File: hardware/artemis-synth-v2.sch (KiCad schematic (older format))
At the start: 41 parts, among them IC1 ATMEGA328P, J1 AVR-ISP-6, J2 CONN JACK STEREO R/A 3PIN 3.5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, SW1 SWITCH_PUSH_CW, SW10 SWITCH_PUSH_CW, SW2 SWITCH_PUSH_CW, SW3 SWITCH_PUSH_CW, SW4 SWITCH_PUSH_CW, SW5 SWITCH_PUSH_CW, SW6 SWITCH_PUSH_CW, SW7 SWITCH_PUSH_CW, SW8 SWITCH_PUSH_CW, SW9 SWITCH_PUSH_CW, U1 MCP4921

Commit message: Updated naming
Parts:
- C1: footprint (none) -> C1V8
- C6: footprint C1 -> C1V8
- D1, D2: footprint (none) -> LED-3MM
- D10, D3, D4, D5, D6, D7, D8, D9: footprint LED-5MM -> LED-3MM
- J2: footprint (none) -> 3-Pin
- R1, R2, R3, R4, R5, R6, R7, R8, R9: footprint (none) -> R4
- RV1: footprint (none) -> THUMBWHEEL_POT_3352T
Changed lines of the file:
@@
-EESchema Schematic File Version 2  date Wed 03 Jul 2013 03:39:44 PM EDT
+EESchema Schematic File Version 2  date Wed 03 Jul 2013 05:09:10 PM EDT
 LIBS:power
 LIBS:device
@@
 LIBS:contrib
 LIBS:valves
-LIBS:mcp49x1
 LIBS:tda2822m
 LIBS:r_us
 LIBS:pot_us
+LIBS:mcp49x1
+LIBS:battery2
+LIBS:artemis-synth-v1-cache
 LIBS:3-pin_audio_jack
-LIBS:artemis-synth-v1-cache
 EELAYER 27 0
 EELAYER END
@@
 F 0 "D4" H 9425 5950 50  0000 C CNN
 F 1 "LED" H 9425 5750 50  0000 C CNN
-F 2 "LED-5MM" H 9425 5850 50  0001 C CNN
+F 2 "LED-3MM" H 9425 5850 50  0001 C CNN
 	1    9425 5850
 	0    1    1    0
@@
 F 0 "D6" H 9875 5950 50  0000 C CNN
 F 1 "LED" H 9875 5750 50  0000 C CNN
-F 2 "LED-5MM" H 9875 5850 50  0001 C CNN
+F 2 "LED-3MM" H 9875 5850 50  0001 C CNN
 	1    9875 5850
 	0    1    1    0
@@
 F 0 "D8" H 10300 5950 50  0000 C CNN
 F 1 "LED" H 10300 5750 50  0000 C CNN
-F 2 "LED-5MM" H 10300 5850 50  0001 C CNN
+F 2 "LED-3MM" H 10300 5850 50  0001 C CNN
 	1    10300 5850
 	0    1    1    0
@@
 F 0 "D10" H 10775 5950 50  0000 C CNN
 F 1 "LED" H 10775 5750 50  0000 C CNN
-F 2 "LED-5MM" H 10775 5850 50  0001 C CNN
+F 2 "LED-3MM" H 10775 5850 50  0001 C CNN
 	1    10775 5850
 	0    1    1    0
@@
 F 0 "D9" H 10775 5450 50  0000 C CNN
 F 1 "LED" H 10775 5250 50  0000 C CNN
-F 2 "LED-5MM" H 10775 5350 50  0001 C CNN
+F 2 "LED-3MM" H 10775 5350 50  0001 C CNN
 	1    10775 5350
 	0    1    1    0
@@
 F 0 "D7" H 10300 5450 50  0000 C CNN
 F 1 "LED" H 10300 5250 50  0000 C CNN
-F 2 "LED-5MM" H 10300 5350 50  0001 C CNN
+F 2 "LED-3MM" H 10300 5350 50  0001 C CNN
 	1    10300 5350
 	0    1    1    0
@@
 F 0 "D5" H 9875 5450 50  0000 C CNN
 F 1 "LED" H 9875 5250 50  0000 C CNN
-F 2 "LED-5MM" H 9875 5350 50  0001 C CNN
+F 2 "LED-3MM" H 9875 5350 50  0001 C CNN
 	1    9875 5350
 	0    1    1    0
@@
 F 0 "D3" H 9425 5450 50  0000 C CNN
 F 1 "LED" H 9425 5250 50  0000 C CNN
-F 2 "LED-5MM" H 9425 5350 50  0001 C CNN
+F 2 "LED-3MM" H 9425 5350 50  0001 C CNN
 	1    9425 5350
 	0    1    1    0
@@
 	-1   0    0    -1
 $EndComp
-Text Label 1688 5375 0    60   ~ 0
+Text Label 3525 5350 0    60   ~ 0
 BT5
-Text Label 1688 5875 0    60   ~ 0
+Text Label 3575 5850 0    60   ~ 0
 BT6
-Text Label 1688 6400 0    60   ~ 0
+Text Label 3575 6375 0    60   ~ 0
 BT7
-Text Label 1688 6950 0    60   ~ 0
+Text Label 3575 6925 0    60   ~ 0
 BT8
-Text Label 1663 7475 0    60   ~ 0
+Text Label 3550 7450 0    60   ~ 0
 BT9
-Text Label 3388 7450 0    60   ~ 0
+Text Label 1825 7475 0    60   ~ 0
 BT4
-Text Label 3413 6925 0    60   ~ 0
+Text Label 1850 6950 0    60   ~ 0
 BT3
-Text Label 3413 6375 0    60   ~ 0
+Text Label 1850 6400 0    60   ~ 0
 BT2
-Text Label 3413 5850 0    60   ~ 0
+Text Label 1850 5875 0    60   ~ 0
 BT1
-Text Label 3363 5350 0    60   ~ 0
+Text Label 1850 5375 0    60   ~ 0
 BT0
 $Comp
@@
 F 0 "D2" H 6100 5975 50  0000 L CNN
 F 1 "TEPT4400" H 6100 5825 50  0000 L CNN
+F 2 "LED-3MM" H 6100 5925 50  0001 C CNN
 	1    5950 5925
 	-1   0    0    -1
@@
 F 0 "R2" H 5405 6100 50  0000 C CNN
 F 1 "1k" H 5400 5950 50  0000 C CNN
+F 2 "R4" H 5400 6050 50  0001 C CNN
 	1    5250 5975
 	-1   0    0    -1
@@
 F 0 "R3" H 5405 6875 50  0000 C CNN
 F 1 "1k" H 5400 6775 50  0000 C CNN
+F 2 "R4" H 5400 6875 50  0001 C CNN
 	1    5250 6750
 	-1   0    0    -1
@@
 F 0 "R5" H 6005 6900 50  0000 C CNN
 F 1 "47k" H 6025 6800 50  0000 C CNN
+F 2 "R4" H 6025 6900 50  0001 C CNN
 	1    5850 6775
 	-1   0    0    -1
@@
 F 0 "R6" H 6755 1725 50  0000 C CNN
 F 1 "100k" H 6800 1600 50  0000 C CNN
+F 2 "R4" H 6800 1700 50  0001 C CNN
 	1    6600 1600
 	1    0    0    -1
@@
 F 0 "R4" H 5905 3375 50  0000 C CNN
 F 1 "10K" H 5900 3225 50  0000 C CNN
+F 2 "R4" H 5900 3325 50  0001 C CNN
 	1    5750 3250
 	1    0    0    -1
@@
 F 0 "R8" V 8550 2600 50  0000 C CNN
 F 1 "1k" V 8450 2600 50  0000 C CNN
+F 2 "R4" V 8550 2600 50  0001 C CNN
 	1    8300 2525
 	0    -1   -1   0
@@
 F 0 "RV1" H 8455 2900 50  0000 C CNN
 F 1 "1k" H 8475 2800 50  0000 C CNN
+F 2 "THUMBWHEEL_POT_3352T" H 8475 2900 50  0001 C CNN
 	1    8650 2850
 	1    0    0    -1
@@
 F 0 "R7" V 7875 2600 50  0000 C CNN
 F 1 "1k" V 7775 2600 50  0000 C CNN
+F 2 "R4" V 7875 2600 50  0001 C CNN
 	1    7625 2525
 	0    -1   -1   0
@@
 F 0 "C6" V 9075 2925 50  0000 L CNN
 F 1 "33uF" V 8975 2825 50  0000 L CNN
-F 2 "C1" H 9075 2850 50  0001 C CNN
+F 2 "C1V8" H 9075 2850 50  0001 C CNN
 	1    9250 2850
 	0    -1   -1   0
@@
 F 0 "R9" H 9700 3275 50  0000 C CNN
 F 1 "47k" H 9725 3175 50  0000 C CNN
+F 2 "R4" H 9725 3275 50  0001 C CNN
 	1    9550 3200
 	1    0    0    -1
@@
 F 0 "C1" H 2450 1675 50  0000 L CNN
 F 1 "10u" H 2450 1575 50  0000 L CNN
+F 2 "C1V8" H 2450 1675 50  0001 C CNN
 	1    2275 1625
 	1    0    0    -1
@@
 F 0 "D1" V 1400 3275 50  0000 C CNN
 F 1 "GREEN" V 1500 3350 50  0000 C CNN
+F 2 "LED-3MM" V 1600 3350 50  0001 C CNN
 	1    1450 3150
 	0    1    1    0
@@
 F 0 "R1" H 1625 3800 50  0000 C CNN
 F 1 "220" H 1650 3700 50  0000 C CNN
+F 2 "R4" H 1650 3800 50  0001 C CNN
 	1    1450 3700
 	1    0    0    -1
@@
 F 0 "J2" H 10950 3200 60  0000 C CNN
 F 1 "CONN JACK STEREO R/A 3PIN 3.5MM" H 11625 3100 60  0000 C CNN
+F 2 "3-Pin" H 11625 3200 60  0001 C CNN
 F 4 "SJ1-3523N" H 10950 2850 60  0001 C CNN "Manufacture Part Number"
 F 5 "CUI Inc." H 10950 2850 60  0001 C CNN "Manufacture"

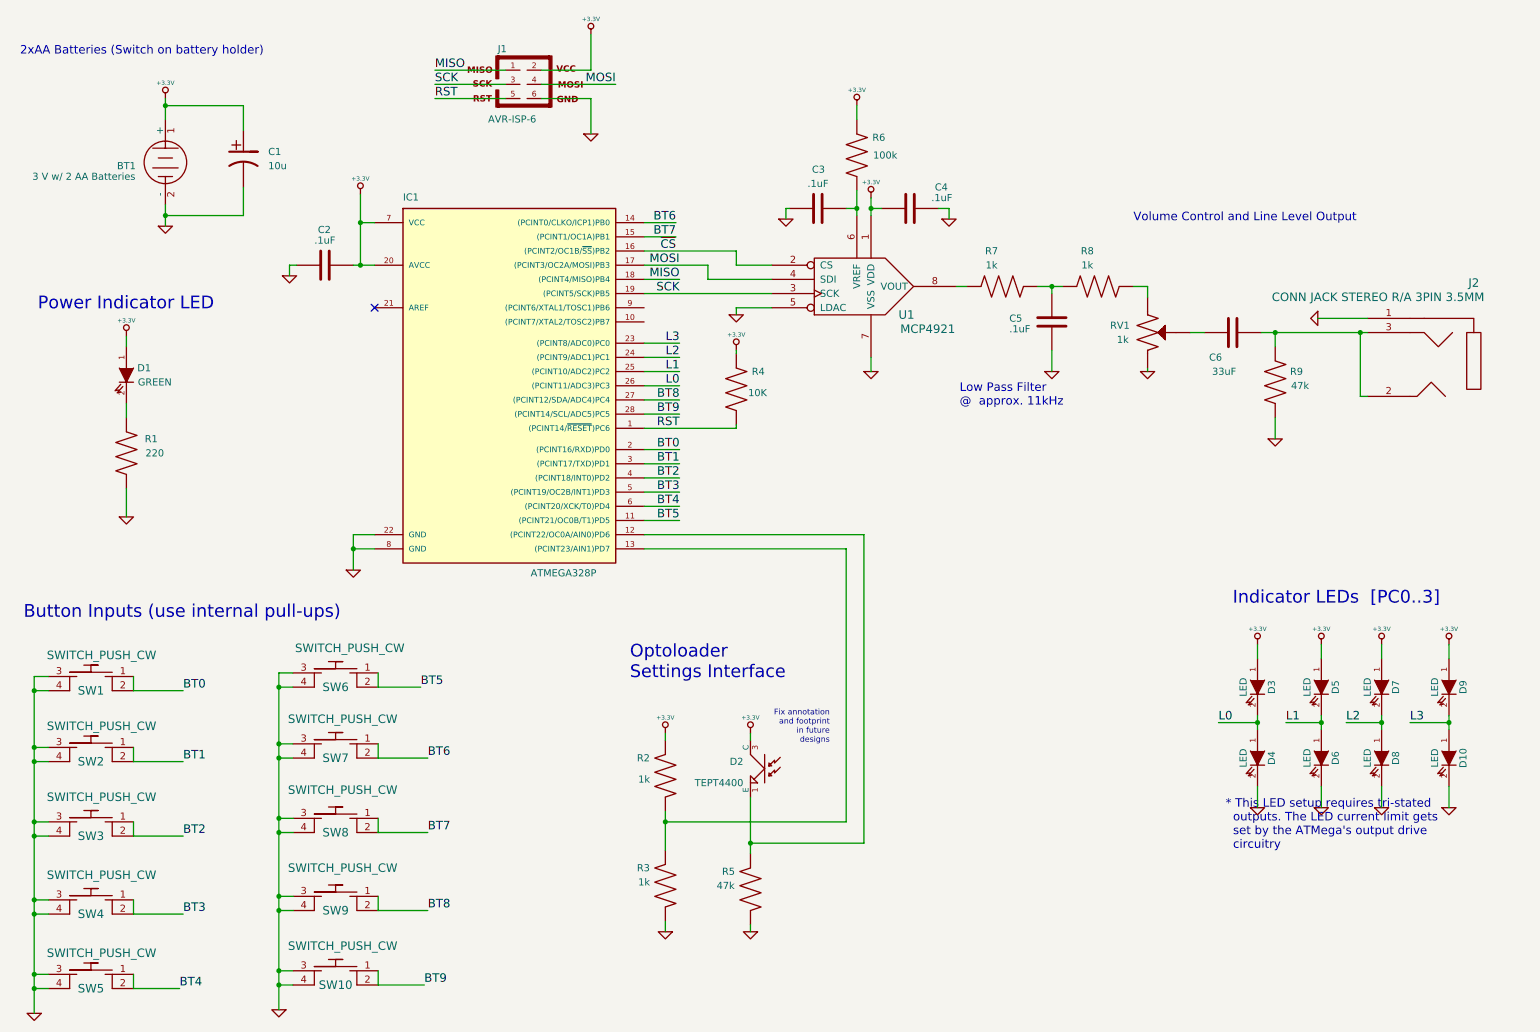
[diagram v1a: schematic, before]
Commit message: fixing up small problems on PCB layout. Finalizing design.
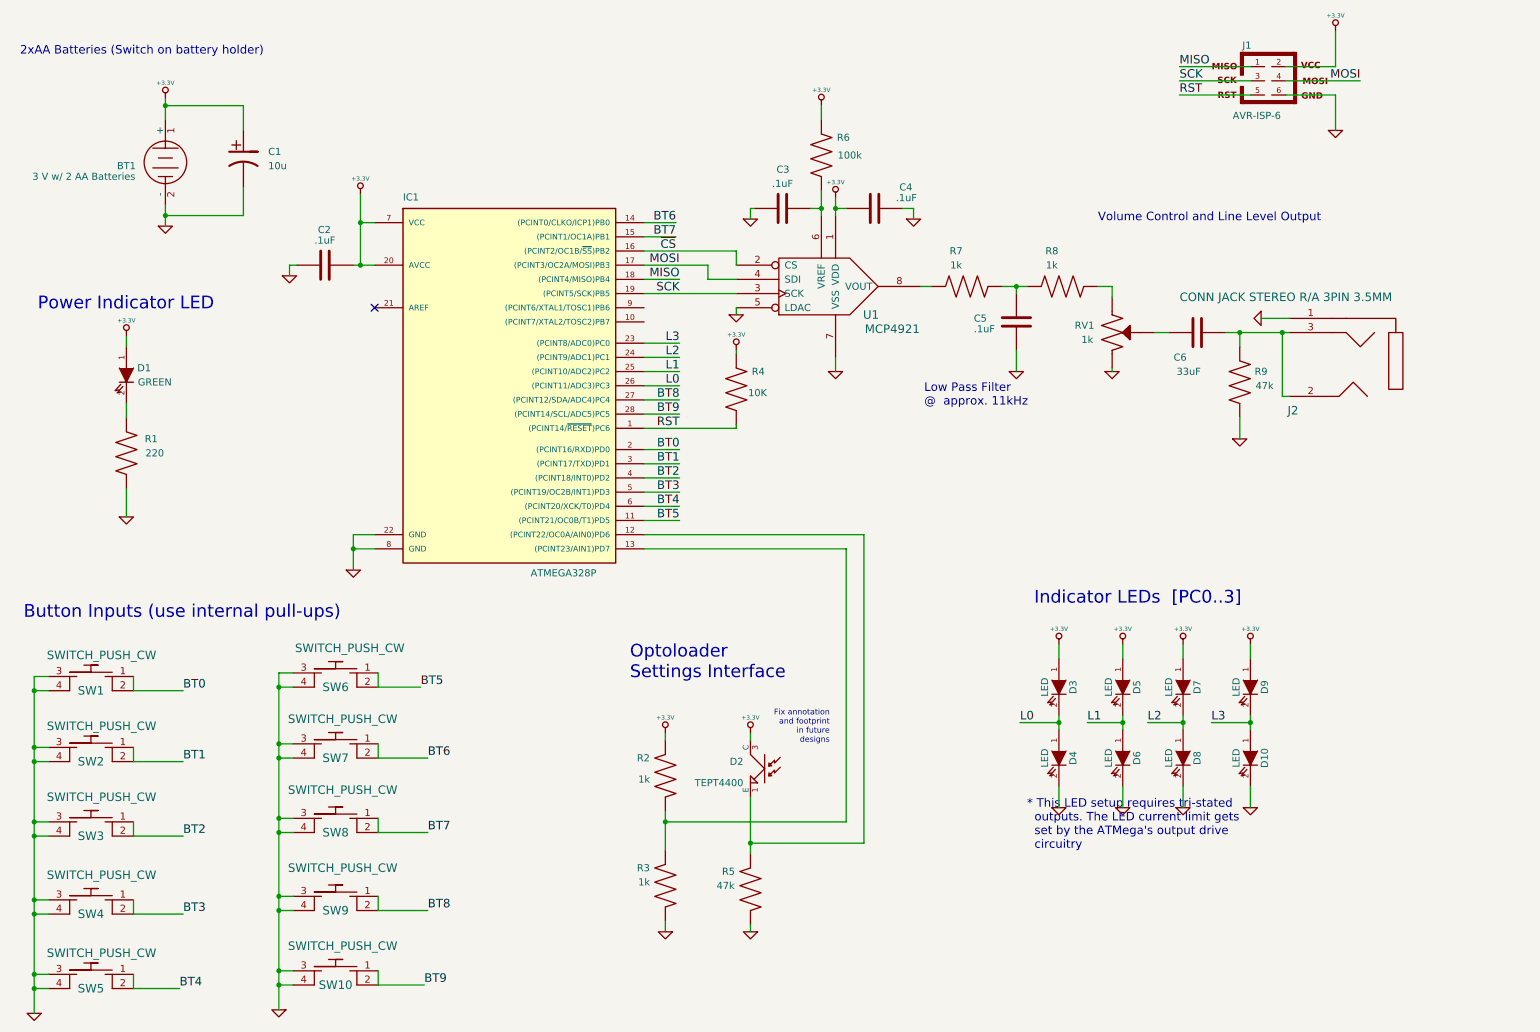
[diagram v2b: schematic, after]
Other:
- moved on the sheet: C3, C4, C5, C6, D10, D3, D4, D5, D6, D7, D8, D9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
